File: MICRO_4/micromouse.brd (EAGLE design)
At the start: 100 x 80 mm, 35 parts

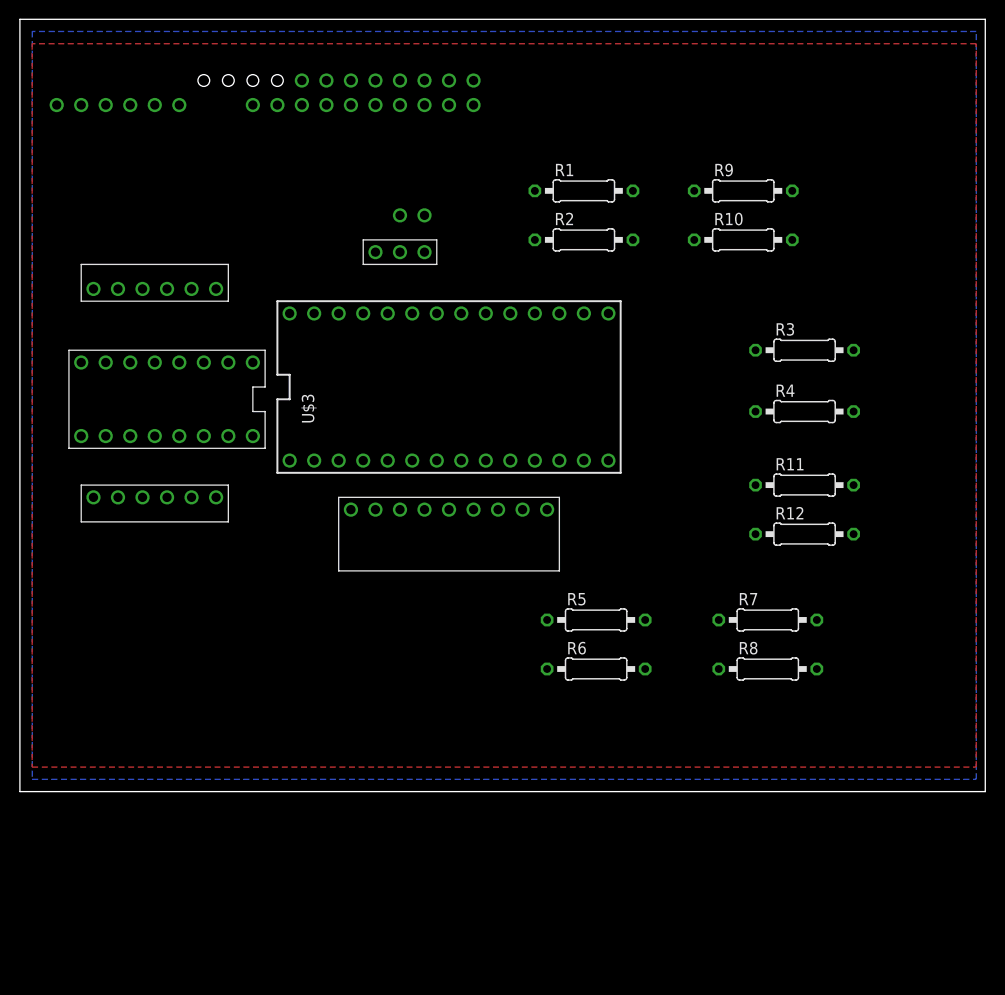
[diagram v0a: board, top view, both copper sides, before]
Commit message: added motor_bracket lbr. need to fix dimension so motor bracket is in mm and board is in mil
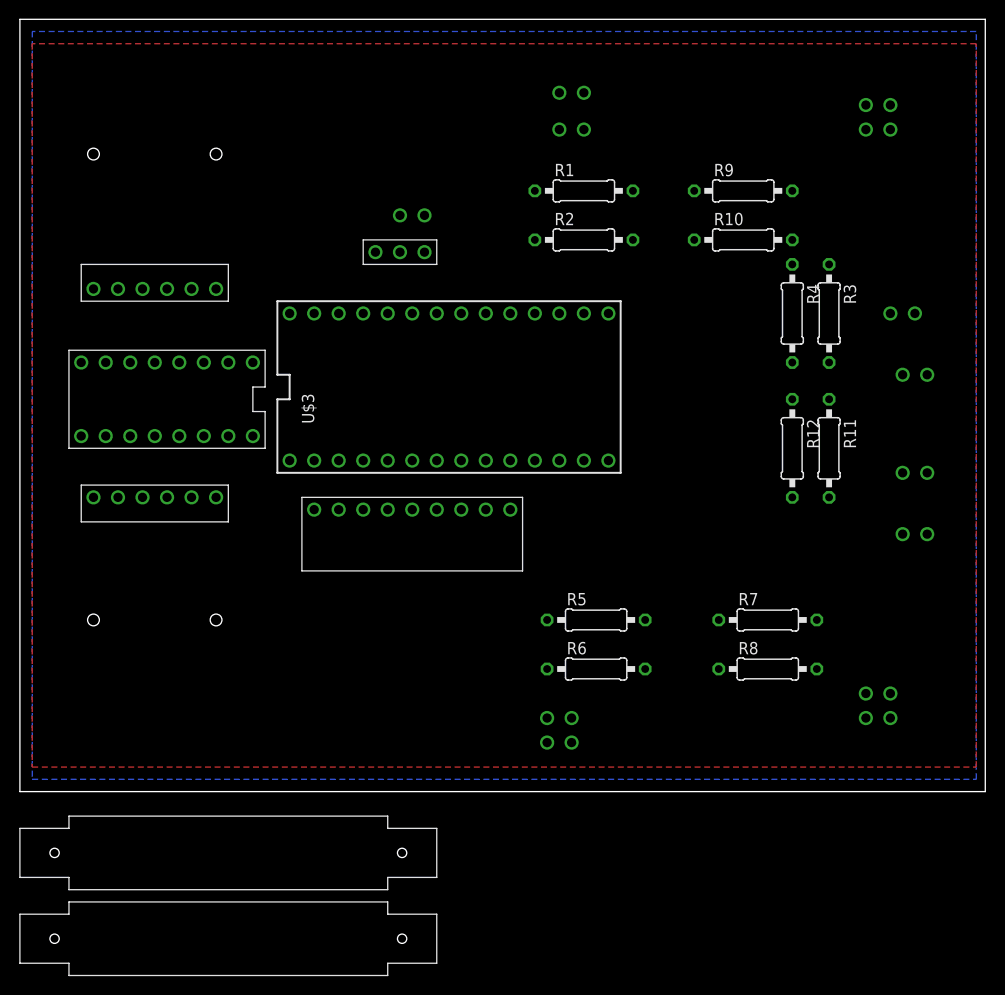
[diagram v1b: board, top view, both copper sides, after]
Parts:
- added U$24, U$25: MOTOR_BRACKET, MOTOR_BRACKET:MOTOR_BRACKET
- moved U$15 105.2 mm to (88.9, 7.62)
- moved U$14 99.6 mm to (87.6, 10.2)
- moved U$12 82.4 mm to (92.7, 43.2)
- moved U$23 78.0 mm to (92.7, 26.7)
- moved U$8 70.8 mm to (55.9, 5.08)
- moved U$22 70.1 mm to (91.4, 33.0)
- moved U$7 66.7 mm to (54.6, 7.62)
- moved U$19 58.3 mm to (7.62, 17.8)
- moved U$18 56.2 mm to (20.3, 17.8)
- moved U$6 55.2 mm to (90.2, 49.5)
- moved U$17 48.5 mm to (88.9, 68.6)
- moved U$16 43.3 mm to (87.6, 71.1)
- moved U$9 31.8 mm to (55.9, 72.4)
- moved U$21 13.7 mm to (7.62, 66.0)
- moved U$5 11.7 mm to (57.1, 68.6)
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
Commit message: changed emitter library to make them more consistent
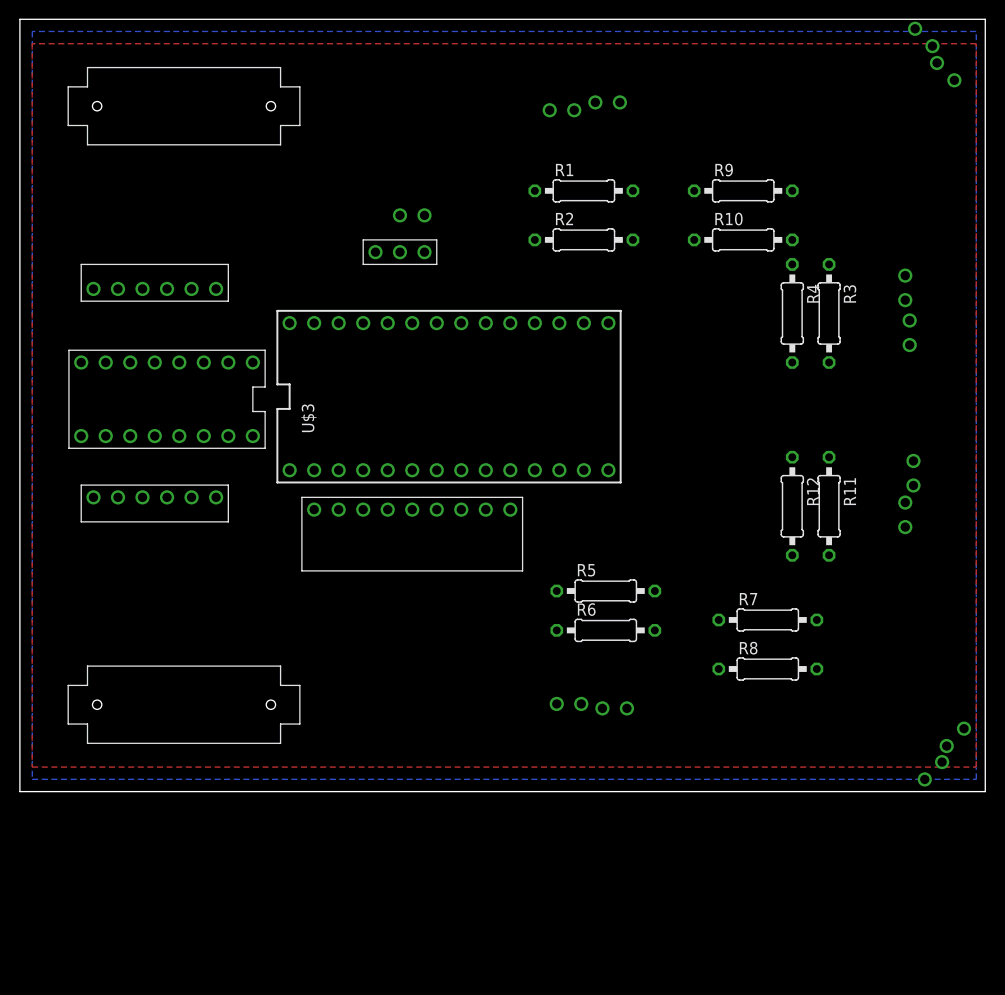
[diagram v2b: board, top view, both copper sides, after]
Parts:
- removed U$20, U$21: THRU_HOLE, THRU_HOLE:THRU_HOLE
- removed U$24, U$25: MOTOR_BRACKET, MOTOR_BRACKET:MOTOR_BRACKET
- U$18, U$19: value THRU_HOLE -> MOTOR_BRACKET; device THRU_HOLE:THRU_HOLE -> MOTOR_BRACKET:MOTOR_BRACKET
- moved U$19 54.0 mm to (17.0, 71.0)
- moved U$14 10.6 mm to (94.6, 2.16), turned to 45 degrees
- moved U$18 9.39 mm to (17.0, 9.00)
- moved U$16 9.22 mm to (93.6, 78.1), turned to 315 degrees
- moved U$17 9.22 mm to (95.9, 74.6), turned to 135 degrees
- moved U$12 9.06 mm to (91.7, 52.2), turned to 90 degrees
- moved U$15 8.25 mm to (96.9, 5.62), turned to 45 degrees
- moved U$7 7.07 mm to (61.6, 8.62)
- moved R11 6.00 mm to (83.8, 29.6)
- moved R12 6.00 mm to (80.0, 29.6)
- moved U$9 5.10 mm to (60.9, 71.4)
- moved R6 4.12 mm to (60.7, 16.7)
- moved U$8 4.12 mm to (56.9, 9.08)
- moved R5 3.16 mm to (60.7, 20.8)
- moved U$6 2.83 mm to (92.2, 47.5), turned to 270 degrees
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
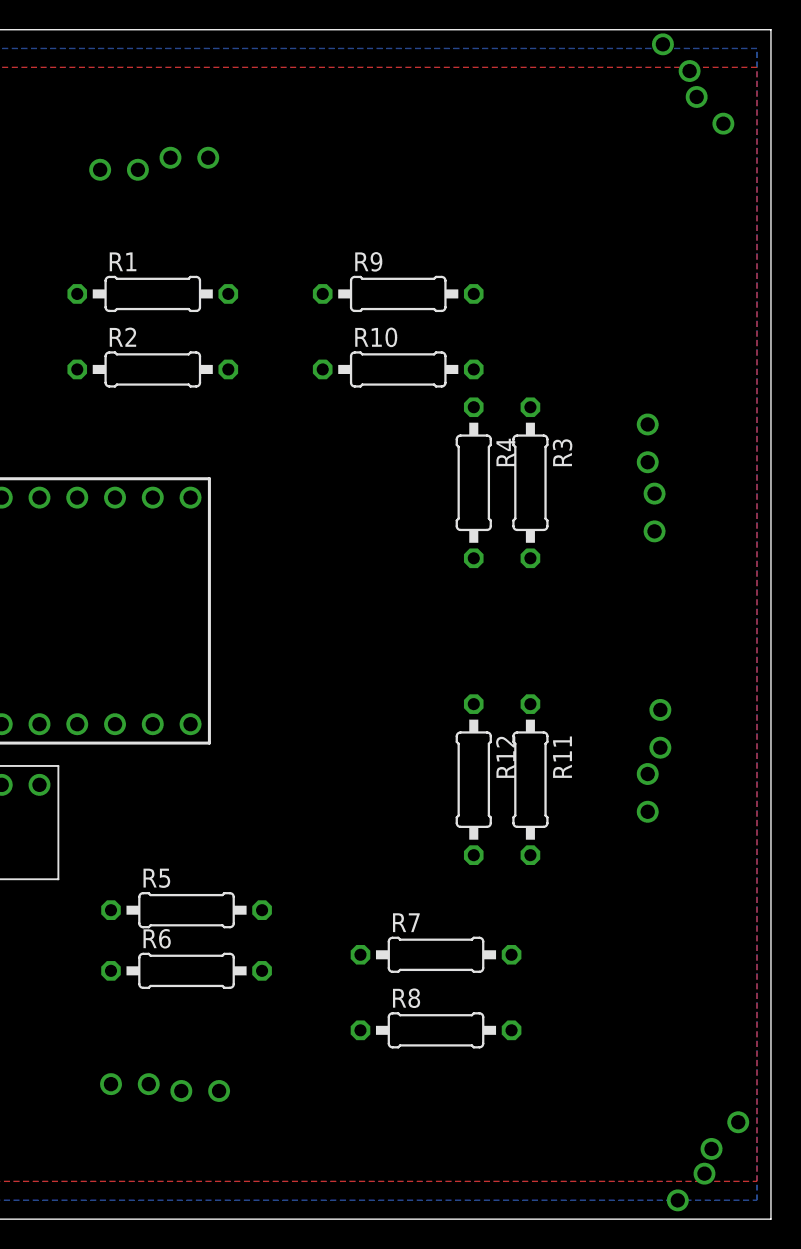
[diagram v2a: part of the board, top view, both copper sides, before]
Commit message: 45 degrees placed
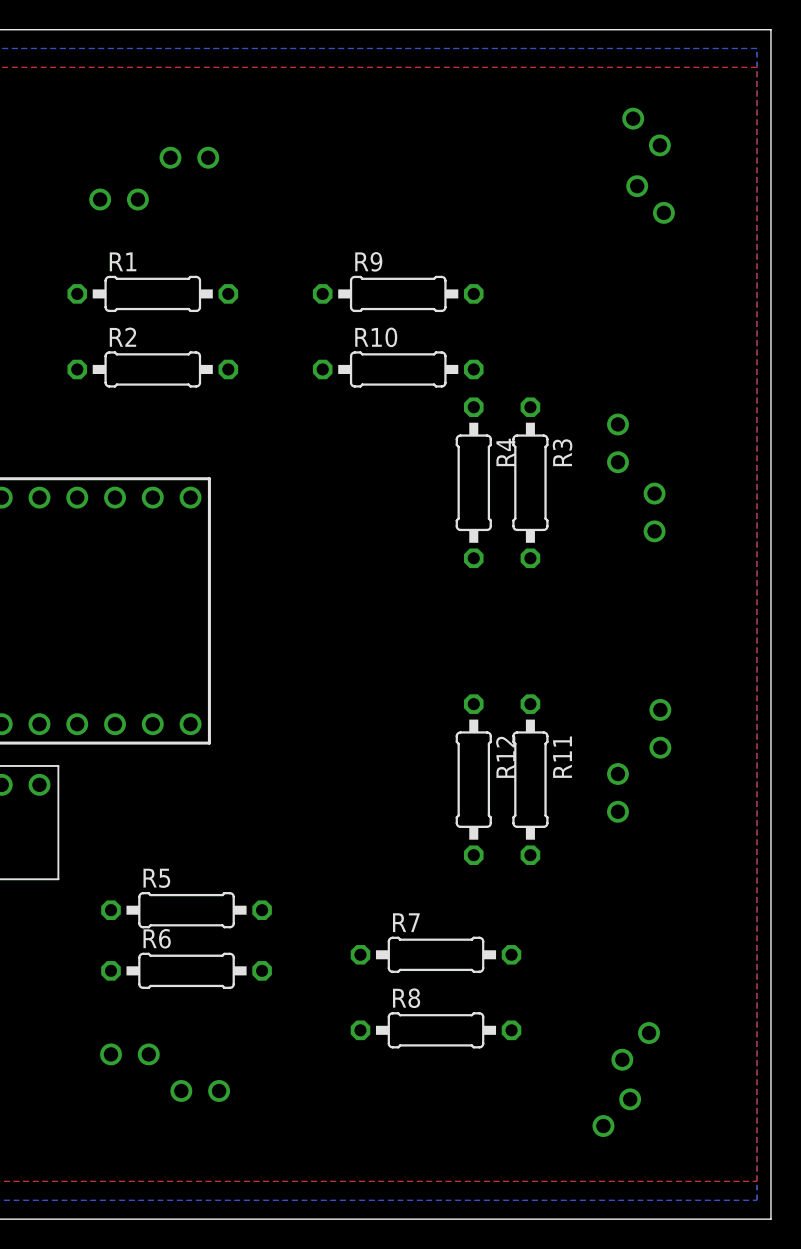
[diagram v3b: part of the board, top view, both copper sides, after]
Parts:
- moved U$15 8.49 mm to (90.9, 11.6)
- moved U$17 7.21 mm to (91.9, 68.6)
- moved U$14 7.07 mm to (89.6, 7.16)
- moved U$16 5.39 mm to (91.6, 73.1)
- moved U$12 2.00 mm to (89.7, 52.2)
- moved U$23 2.00 mm to (89.7, 28.7)
- moved U$5 2.00 mm to (56.1, 68.6)
- moved U$8 2.00 mm to (56.9, 11.1)
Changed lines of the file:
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@@
 <element name="U$10" library="VOLTAGE_REGULATOR" package="VOLTAGE_REGULATOR" value="VOLTAGE_REGULATOR" x="39.37" y="55.88"/>
 <element name="U$11" library="Battery_input" package="BATTERY_INPUT" value="BATTERY_INPUT" x="40.64" y="59.69" rot="R180"/>
-<element name="U$12" library="IR_RECIEVER" package="IR_RECIEVER" value="IR_RECIEVER" x="91.71" y="52.18" rot="R90"/>
+<element name="U$12" library="IR_RECIEVER" package="IR_RECIEVER" value="IR_RECIEVER" x="89.71" y="52.18" rot="R90"/>
 <element name="U$13" library="IMU" package="IMU" value="IMU" x="45.72" y="27.94" rot="R270"/>
-<element name="U$14" library="IR_EMITTER" package="IR_EMITTER" value="IR_EMITTER" x="94.63" y="2.16" rot="R45"/>
-<element name="U$15" library="IR_RECIEVER" package="IR_RECIEVER" value="IR_RECIEVER" x="96.9" y="5.62" rot="R45"/>
-<element name="U$16" library="IR_EMITTER" package="IR_EMITTER" value="IR_EMITTER" x="93.63" y="78.12" rot="R315"/>
-<element name="U$17" library="IR_RECIEVER" package="IR_RECIEVER" value="IR_RECIEVER" x="95.9" y="74.58" rot="R135"/>
+<element name="U$14" library="IR_EMITTER" package="IR_EMITTER" value="IR_EMITTER" x="89.63" y="7.16" rot="R45"/>
+<element name="U$15" library="IR_RECIEVER" package="IR_RECIEVER" value="IR_RECIEVER" x="90.9" y="11.62" rot="R45"/>
+<element name="U$16" library="IR_EMITTER" package="IR_EMITTER" value="IR_EMITTER" x="91.63" y="73.12" rot="R315"/>
+<element name="U$17" library="IR_RECIEVER" package="IR_RECIEVER" value="IR_RECIEVER" x="91.9" y="68.58" rot="R135"/>
 <element name="U$2" library="MOTOR_ENCODER" package="MOTOR_ENCODER" value="MOTOR_ENCODER" x="11.43" y="31.75" rot="R90"/>
 <element name="U$22" library="IR_EMITTER" package="IR_EMITTER" value="IR_EMITTER" x="92.56" y="32.98" rot="R270"/>
-<element name="U$23" library="IR_RECIEVER" package="IR_RECIEVER" value="IR_RECIEVER" x="91.71" y="28.67" rot="R90"/>
+<element name="U$23" library="IR_RECIEVER" package="IR_RECIEVER" value="IR_RECIEVER" x="89.71" y="28.67" rot="R90"/>
 <element name="U$3" library="Teensy_3_and_LC_Series_Boards_v1.4" package="TEENSY_3.0-3.2&amp;LC_DIL" value="TEENSY_3.1-3.2_DIL" x="44.45" y="40.91" rot="R90"/>
 <element name="U$4" library="motor_driver" package="MOTOR_DRIVER" value="MOTOR_DRIVER" x="17.78" y="40.64" rot="R270"/>
-<element name="U$5" library="IR_RECIEVER" package="IR_RECIEVER" value="IR_RECIEVER" x="56.15" y="70.58"/>
+<element name="U$5" library="IR_RECIEVER" package="IR_RECIEVER" value="IR_RECIEVER" x="56.15" y="68.58"/>
 <element name="U$6" library="IR_EMITTER" package="IR_EMITTER" value="IR_EMITTER" x="92.17" y="47.53" rot="R270"/>
 <element name="U$7" library="IR_EMITTER" package="IR_EMITTER" value="IR_EMITTER" x="61.61" y="8.62"/>
-<element name="U$8" library="IR_RECIEVER" package="IR_RECIEVER" value="IR_RECIEVER" x="56.88" y="9.08"/>
+<element name="U$8" library="IR_RECIEVER" package="IR_RECIEVER" value="IR_RECIEVER" x="56.88" y="11.08"/>
 <element name="U$9" library="IR_EMITTER" package="IR_EMITTER" value="IR_EMITTER" x="60.88" y="71.39"/>
 <element name="U$18" library="MOTOR_BRACKET" package="MOTOR_BRACKET" value="MOTOR_BRACKET" x="17" y="9"/>
@@
 <contactref element="U$3" pad="14/A0"/>
 <wire x1="55.61" y1="16.7" x2="58.42" y2="48.53" width="0" layer="19" extent="1-1"/>
-<wire x1="58.15" y1="9.08" x2="55.61" y2="16.7" width="0" layer="19" extent="1-1"/>
+<wire x1="58.15" y1="11.08" x2="55.61" y2="16.7" width="0" layer="19" extent="1-1"/>
 </signal>
 <signal name="N$24">
@@
 <contactref element="R4" pad="1"/>
 <contactref element="U$3" pad="15/A1"/>
-<wire x1="80.01" y1="54.61" x2="91.71" y2="53.45" width="0" layer="19" extent="1-1"/>
+<wire x1="80.01" y1="54.61" x2="89.71" y2="53.45" width="0" layer="19" extent="1-1"/>
 <wire x1="55.88" y1="48.53" x2="80.01" y2="54.61" width="0" layer="19" extent="1-1"/>
 </signal>
@@
 <contactref element="R2" pad="1"/>
 <contactref element="U$3" pad="16/A2"/>
-<wire x1="53.34" y1="57.15" x2="57.42" y2="70.58" width="0" layer="19" extent="1-1"/>
+<wire x1="53.34" y1="57.15" x2="57.42" y2="68.58" width="0" layer="19" extent="1-1"/>
 <wire x1="53.34" y1="48.53" x2="53.34" y2="57.15" width="0" layer="19" extent="1-1"/>
 </signal>
@@
 <contactref element="R7" pad="1"/>
 <contactref element="U$14" pad="EMI_ANO"/>
-<wire x1="72.39" y1="17.78" x2="93.731971875" y2="1.261971875" width="0" layer="19" extent="1-1"/>
+<wire x1="72.39" y1="17.78" x2="88.731971875" y2="6.261971875" width="0" layer="19" extent="1-1"/>
 </signal>
 <signal name="N$9">
@@
 <contactref element="R9" pad="1"/>
 <contactref element="U$16" pad="EMI_ANO"/>
-<wire x1="69.85" y1="62.23" x2="92.731971875" y2="79.018025" width="0" layer="19" extent="1-1"/>
+<wire x1="69.85" y1="62.23" x2="90.731971875" y2="74.018025" width="0" layer="19" extent="1-1"/>
 </signal>
 <signal name="N$8">
@@
 <contactref element="R8" pad="1"/>
 <contactref element="U$3" pad="22/A8"/>
-<wire x1="72.39" y1="12.7" x2="97.798025" y2="6.518025" width="0" layer="19" extent="1-1"/>
+<wire x1="72.39" y1="12.7" x2="91.798025" y2="12.518025" width="0" layer="19" extent="1-1"/>
 <wire x1="38.1" y1="48.53" x2="72.39" y2="12.7" width="0" layer="19" extent="1-1"/>
 </signal>
@@
 <contactref element="R10" pad="1"/>
 <contactref element="U$3" pad="23/A9"/>
-<wire x1="69.85" y1="57.15" x2="95.001971875" y2="75.478025" width="0" layer="19" extent="1-1"/>
+<wire x1="69.85" y1="57.15" x2="91.001971875" y2="69.478025" width="0" layer="19" extent="1-1"/>
 <wire x1="35.56" y1="48.53" x2="69.85" y2="57.15" width="0" layer="19" extent="1-1"/>
 </signal>
@@
 <contactref element="R12" pad="1"/>
 <contactref element="U$3" pad="17/A3"/>
-<wire x1="80.01" y1="34.64" x2="91.71" y2="29.94" width="0" layer="19" extent="1-1"/>
+<wire x1="80.01" y1="34.64" x2="89.71" y2="29.94" width="0" layer="19" extent="1-1"/>
 <wire x1="50.8" y1="48.53" x2="80.01" y2="34.64" width="0" layer="19" extent="1-1"/>
 </signal>
